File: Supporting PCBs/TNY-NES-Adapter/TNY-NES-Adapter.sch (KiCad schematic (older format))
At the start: 2 parts, among them P1 72-Pin Connector, P2 72-Pin Connector

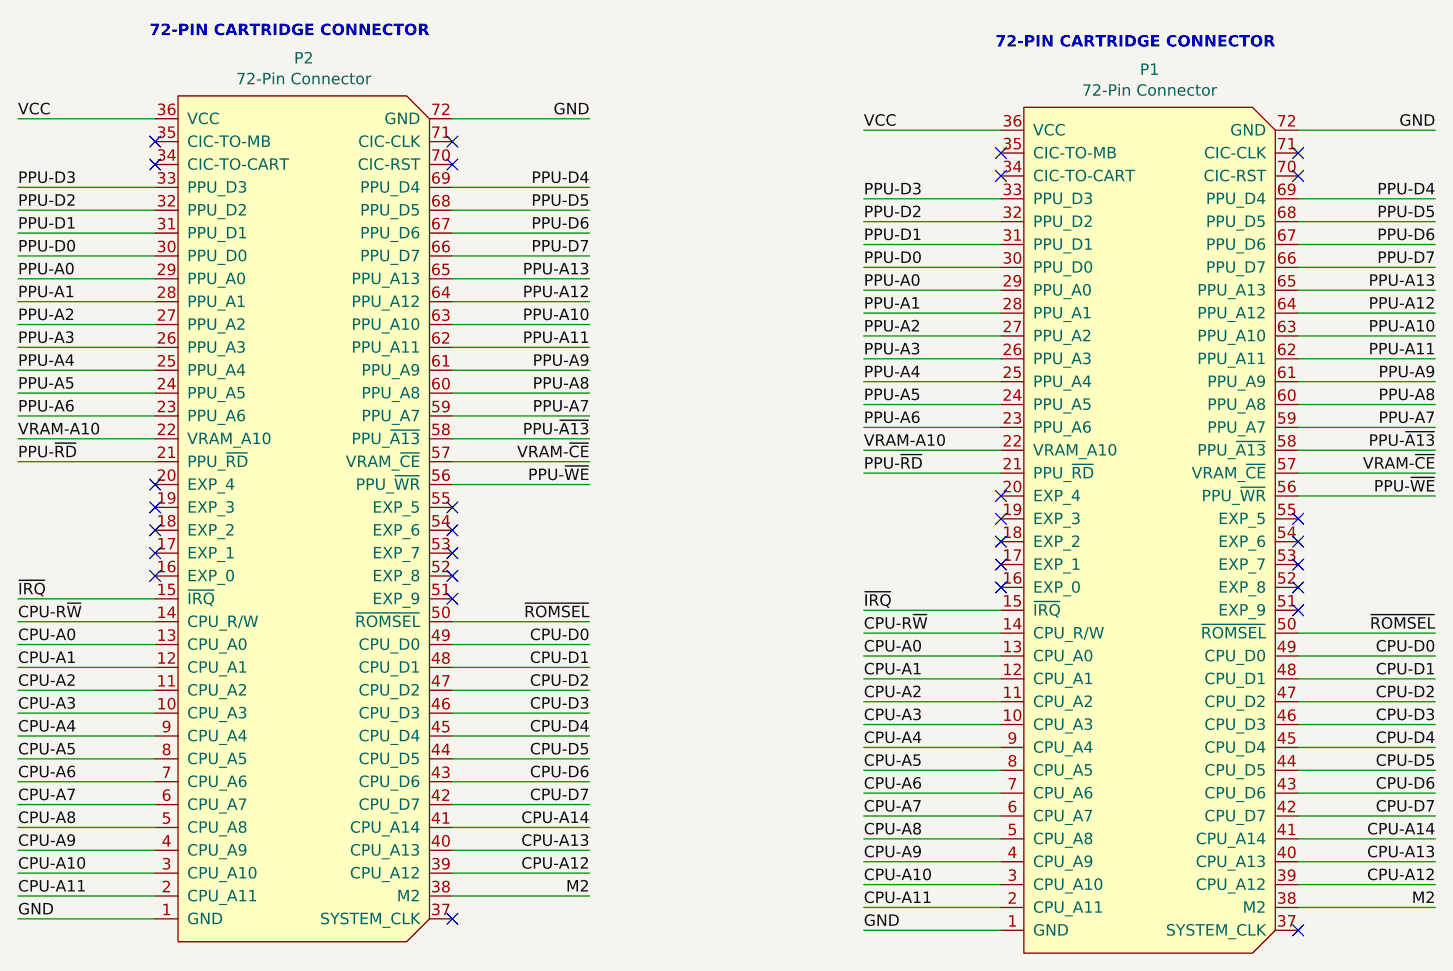
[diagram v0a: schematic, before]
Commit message: + Motherboard is now V1.0 + Redesigned ScreenReg for improved reliability + Added both versions of ChargeBoost + Remove now redundant files/directories
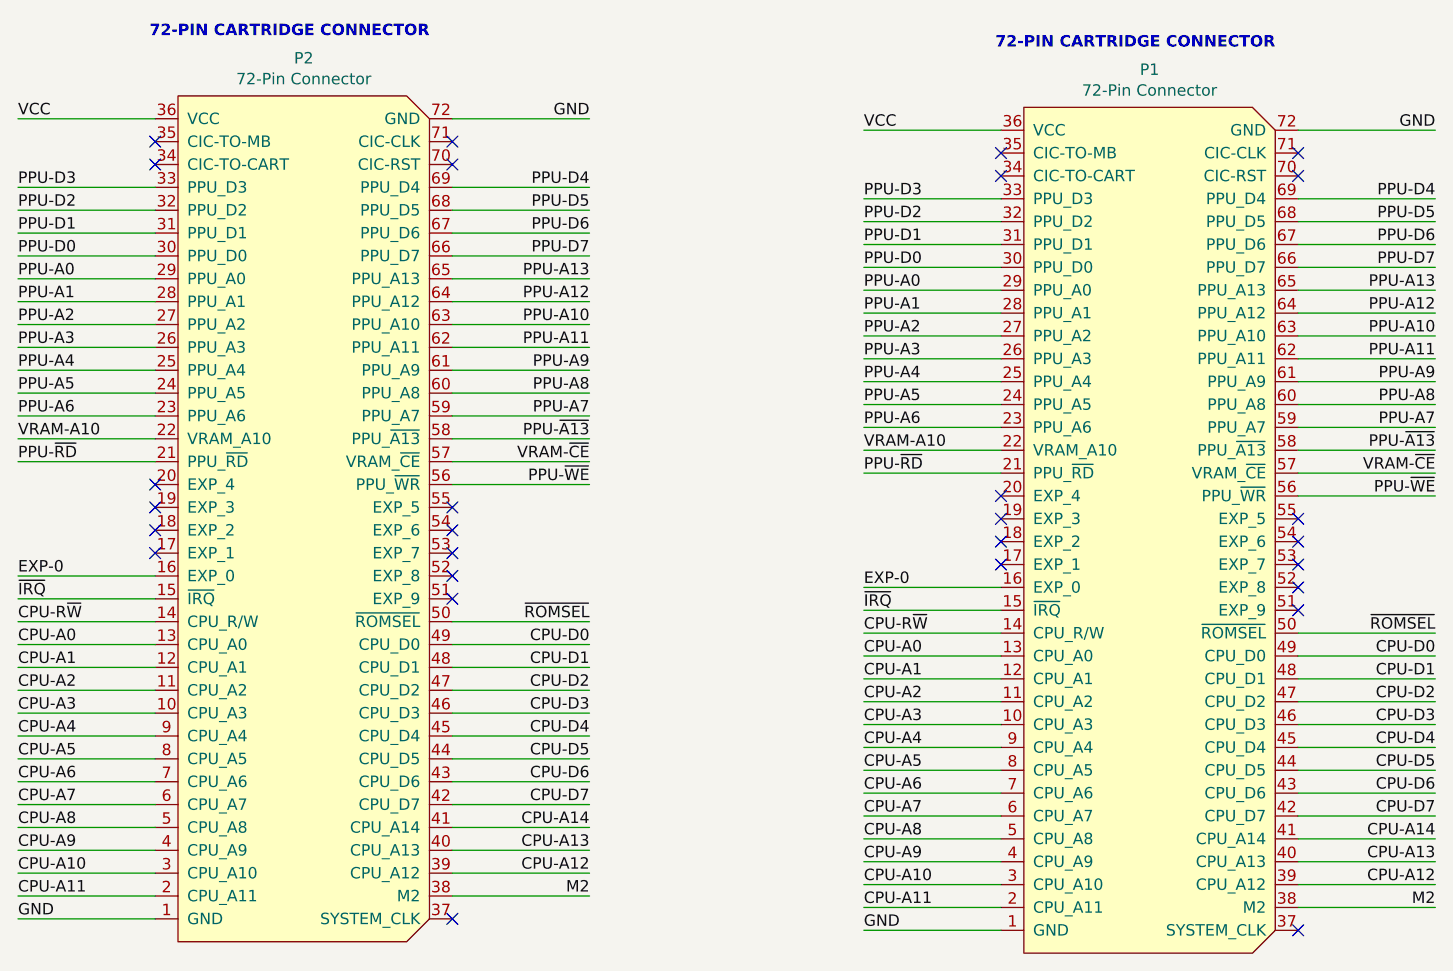
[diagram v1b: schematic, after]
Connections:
- net EXP-0: now reaches P1.16 (EXP_0)
- net EXP-0: now also P2.16 (EXP_0)
- no-connect marks 30 -> 28
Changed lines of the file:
@@
 NoConn ~ 6400 3850
 NoConn ~ 6400 3950
-NoConn ~ 6400 4050
 NoConn ~ 7700 3750
 NoConn ~ 7700 3850
@@
 NoConn ~ 2700 3800
 NoConn ~ 2700 3900
-NoConn ~ 2700 4000
 NoConn ~ 4000 3700
 NoConn ~ 4000 3800
@@
 NoConn ~ 4000 5500
 NoConn ~ 7700 5550
+Text Label 5800 4050 0    50   ~ 0
+EXP-0
+Wire Wire Line
+	6400 4050 5800 4050
+Text Label 2100 4000 0    50   ~ 0
+EXP-0
+Wire Wire Line
+	2700 4000 2100 4000
 $EndSCHEMATC
